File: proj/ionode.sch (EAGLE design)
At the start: 34 parts, among them J2 USB-BAMPHENOL-MICRO, U1 ATMEGA1284P-MU44-VQFN, U4 FT232RQFN32, U5 SN74LVC1G125SOT23-5, U6 SN74LVC1G125SOT23-5, U7 3.3V, X1 10MHz

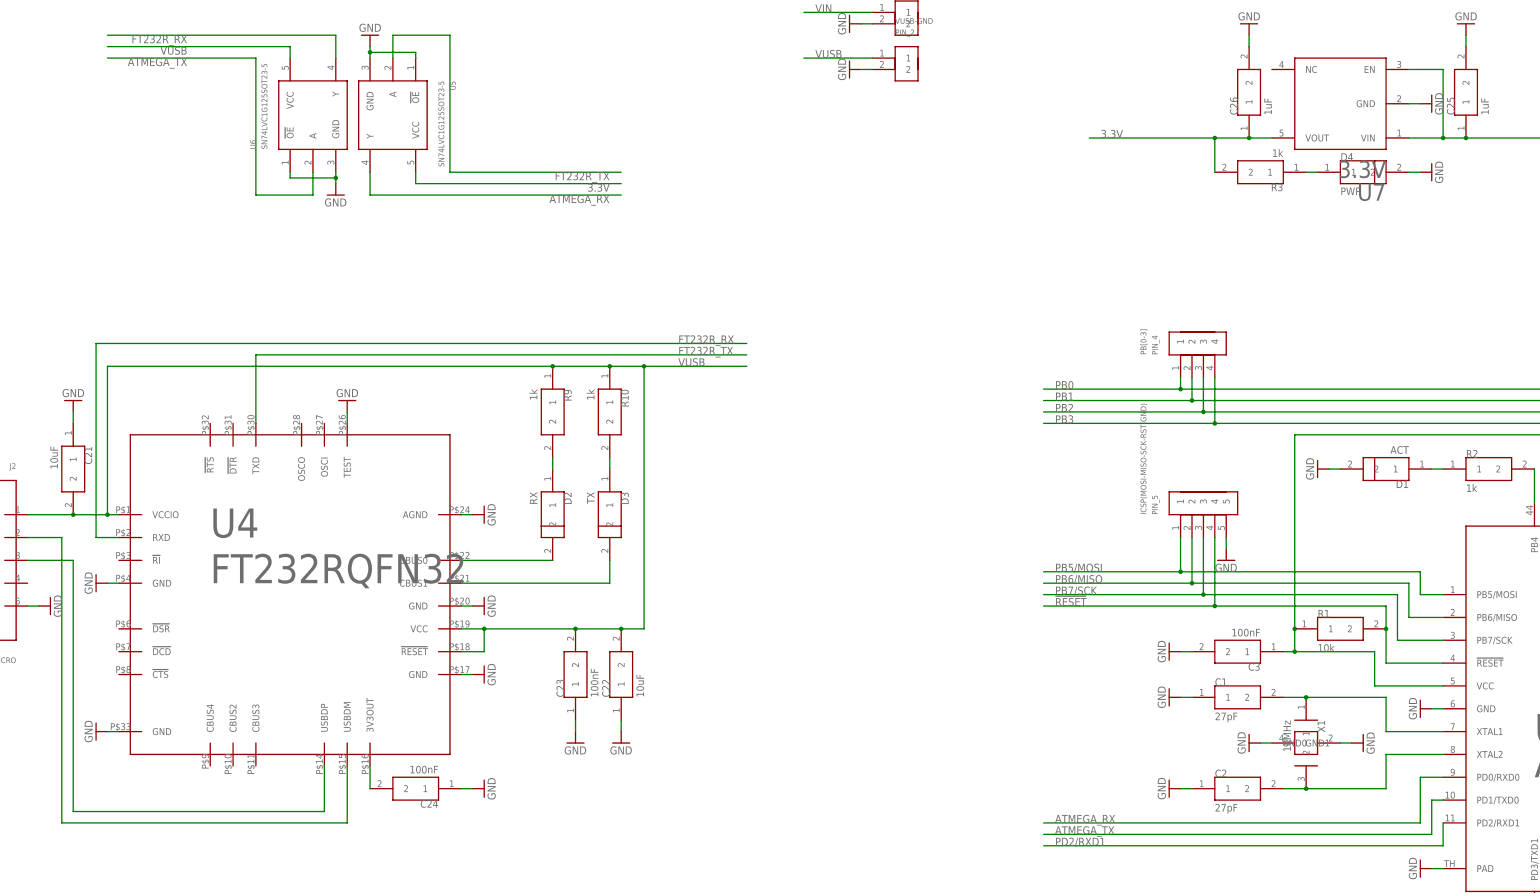
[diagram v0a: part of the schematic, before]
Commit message: Improved reference designators on ionode
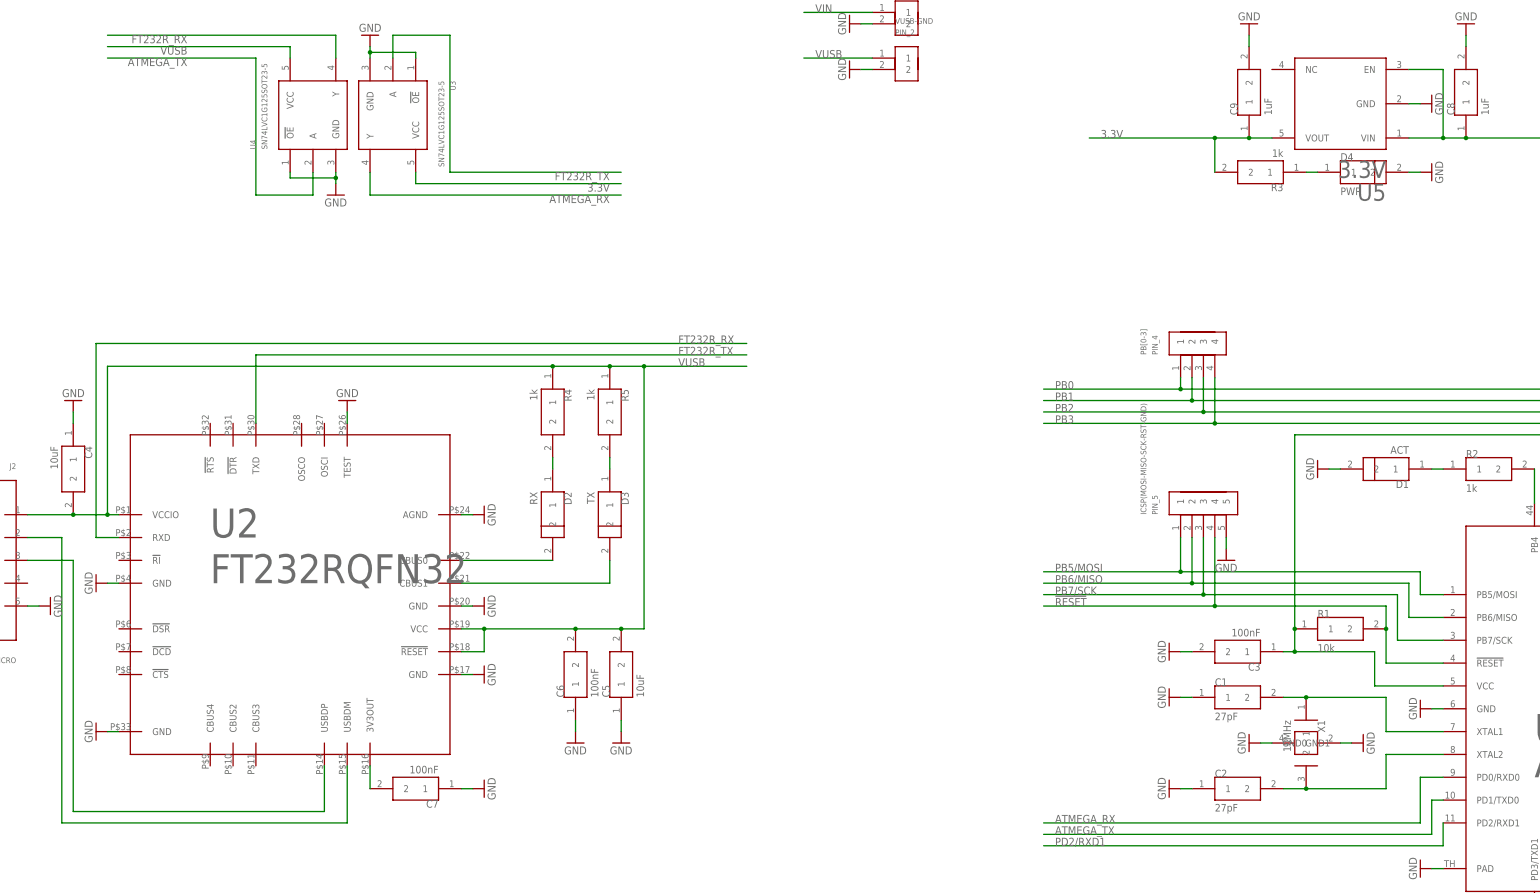
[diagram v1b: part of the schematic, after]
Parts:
- removed U6: SN74LVC1G125SOT23-5, dooba:SN74LVC1G125SOT23-5
- removed U7: 3.3V, dooba:LP3985SOT23-5
- added U2: FT232RQFN32, dooba:FT232RQFN32
- added U3: SN74LVC1G125SOT23-5, dooba:SN74LVC1G125SOT23-5
- U4: value FT232RQFN32 -> SN74LVC1G125SOT23-5; device dooba:FT232RQFN32 -> dooba:SN74LVC1G125SOT23-5
- U5: value SN74LVC1G125SOT23-5 -> 3.3V; device dooba:SN74LVC1G125SOT23-5 -> dooba:LP3985SOT23-5
- renumbered C21 to C4, C22 to C5, C23 to C6, C24 to C7, C25 to C8, C26 to C9, R10 to R5, R9 to R4
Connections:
- net 3.3V: now also U3.VCC, U5.VOUT; no longer U5.VCC, U7.VOUT
- net ATMEGA_RX: now also U3.Y; no longer U5.Y
- net ATMEGA_TX: now also U4.A; no longer U6.A
- net FT232R_RX: now also U2.RXD, U4.Y; no longer U4.RXD, U6.Y
- net FT232R_TX: now also U2.TXD, U3.A; no longer U4.TXD, U5.A
- net GND: now also U2.AGND, U2.GND@17, U2.GND@20, U2.GND@4, U2.GND@PAD, U2.TEST, U3.!OE, U3.GND, U4.!OE, U4.GND; no longer U4.AGND, U4.GND@17, U4.GND@20, U4.GND@4, U4.GND@PAD, U4.TEST, U5.!OE, U6.!OE, U6.GND, U7.GND
- net N$21: now also U2.3V3OUT; no longer U4.3V3OUT
- net N$22: now also U2.CBUS0; no longer U4.CBUS0
- net N$23: now also U2.CBUS1; no longer U4.CBUS1
- net N$26: now also U2.USBDM; no longer U4.USBDM
- net N$27: now also U2.USBDP; no longer U4.USBDP
- net VIN: now also U5.EN, U5.VIN; no longer U7.EN, U7.VIN
- net VUSB: now also U2.!RESET, U2.VCC, U2.VCCIO; no longer U4.!RESET, U4.VCCIO, U6.VCC
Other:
- moved on the sheet: U5

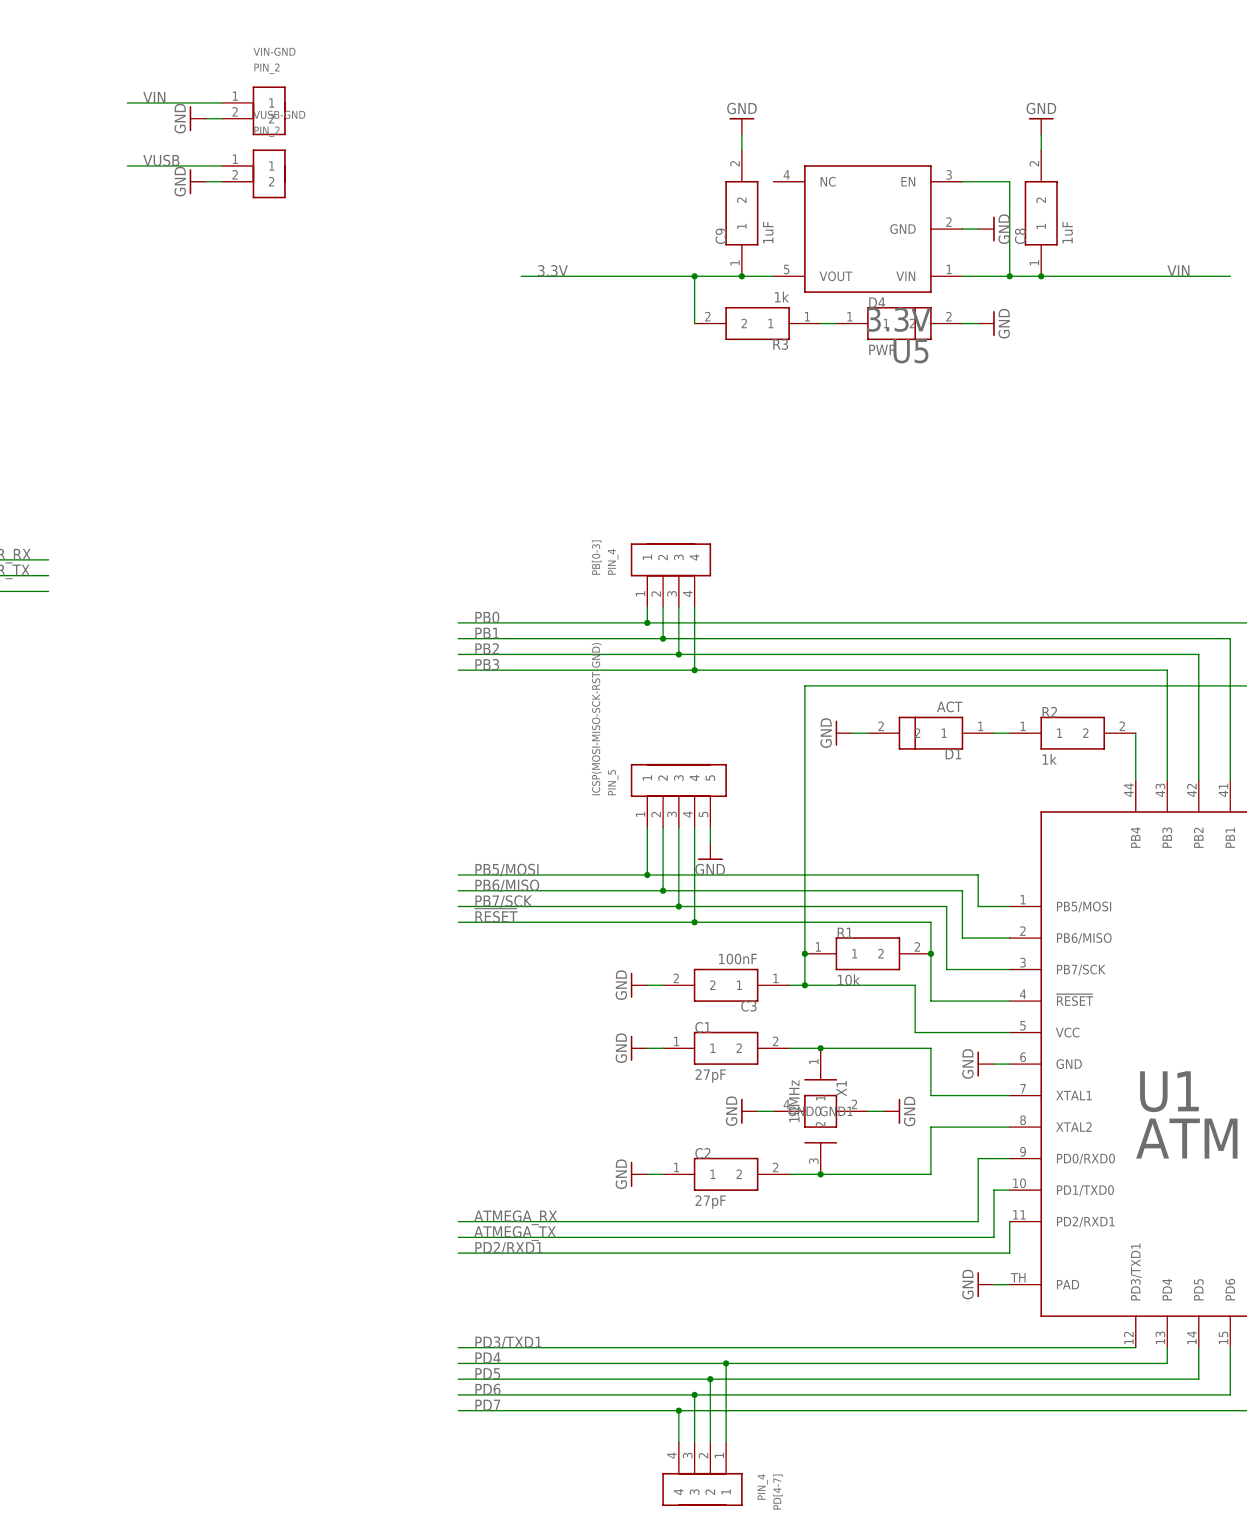
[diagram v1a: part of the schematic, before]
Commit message: Added DRU file for ZhongFeng PCBA Added 0402 footprint Added SMD Jumper footprint Added SMD Jumper to ioNode for VIN - VUSB Upgraded most 0805 parts on ioNode to 0402 Added USART1 TX/RX breakout on ioNode Upgraded ioNode board to better use ZFPCBA DRU
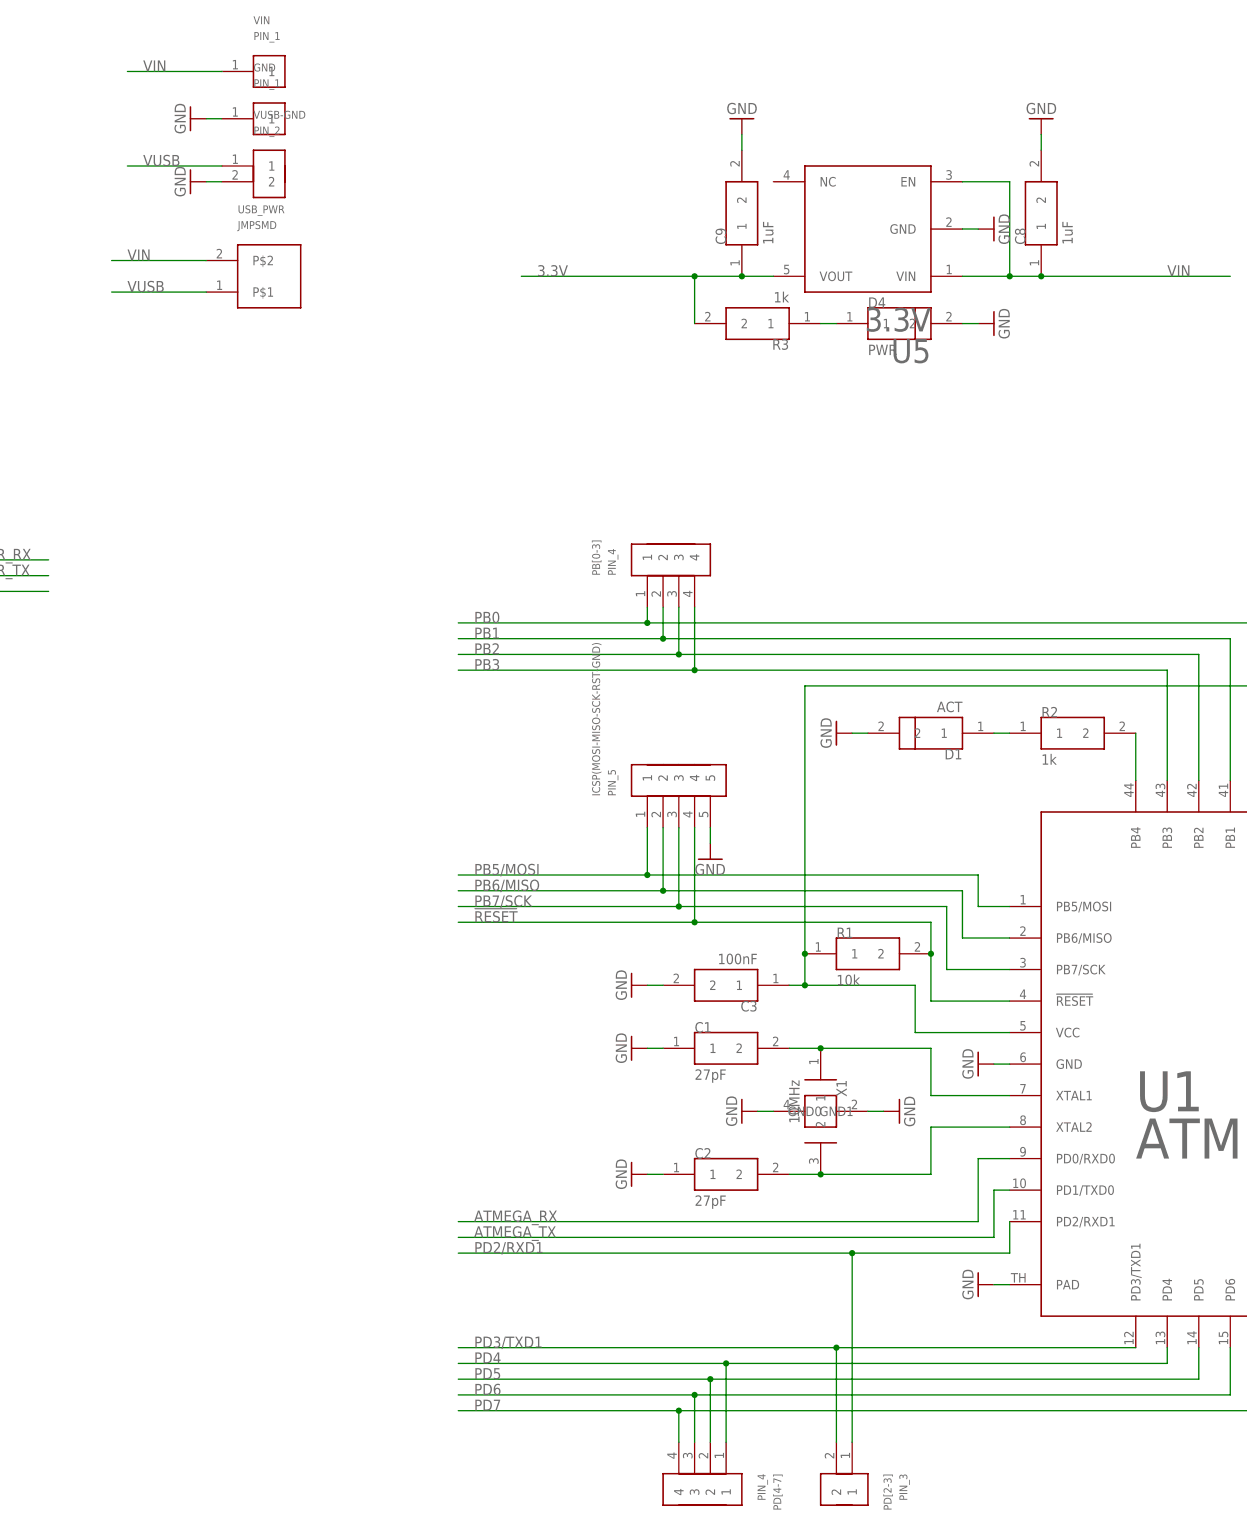
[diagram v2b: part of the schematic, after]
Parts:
- removed VIN-GND: PIN_2, dooba:PIN_2
- added GND, VIN: PIN_1, dooba:PIN_1
- added PIN_3: PD[2-3], dooba:PIN_2
- added USB_PWR: JMPSMD, dooba:JMPSMD
- C1, C2, C3, C6, C7, C8, C9: device dooba:CAP0805 -> dooba:CAP0402
- D1, D2, D3, D4: device dooba:LED0805 -> dooba:LED0402
- R1, R2, R3, R4, R5: device dooba:RES0805 -> dooba:RES0402
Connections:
- net GND: now also GND.1; no longer VIN-GND.2
- net PD2/RXD1: now also PIN_3.1
- net PD3/TXD1: now also PIN_3.2
- net VIN: now also USB_PWR.P$2, VIN.1; no longer VIN-GND.1
- net VUSB: now also USB_PWR.P$1
